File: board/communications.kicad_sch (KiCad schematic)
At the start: 8 parts, among them J1 RJ45_LED_Shielded, U3 ATA6561, U5 ATA6561

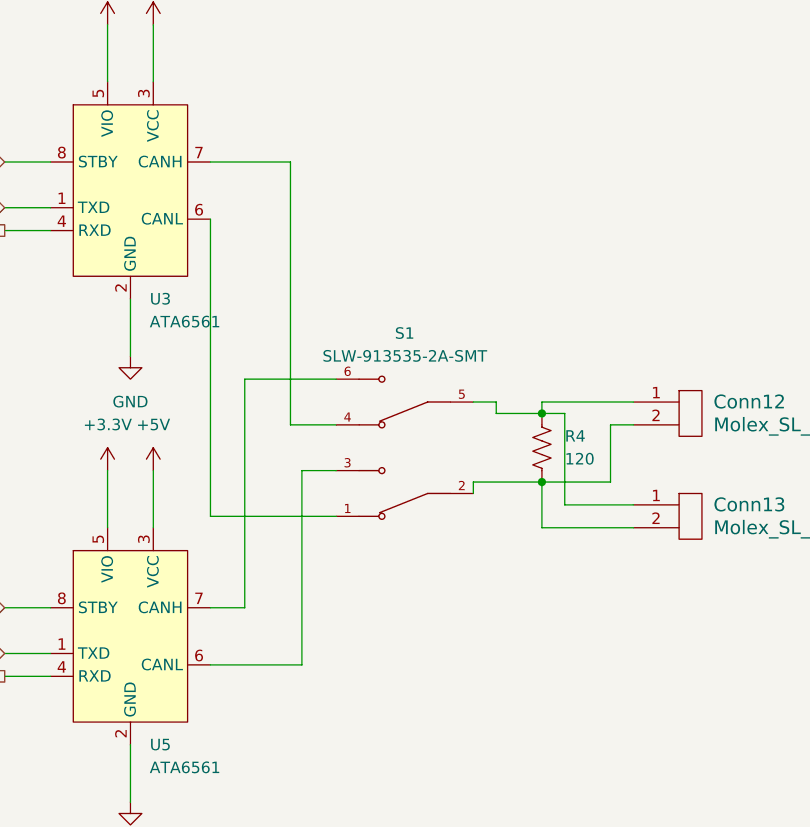
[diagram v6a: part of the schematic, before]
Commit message: Equalized traces, text resizing
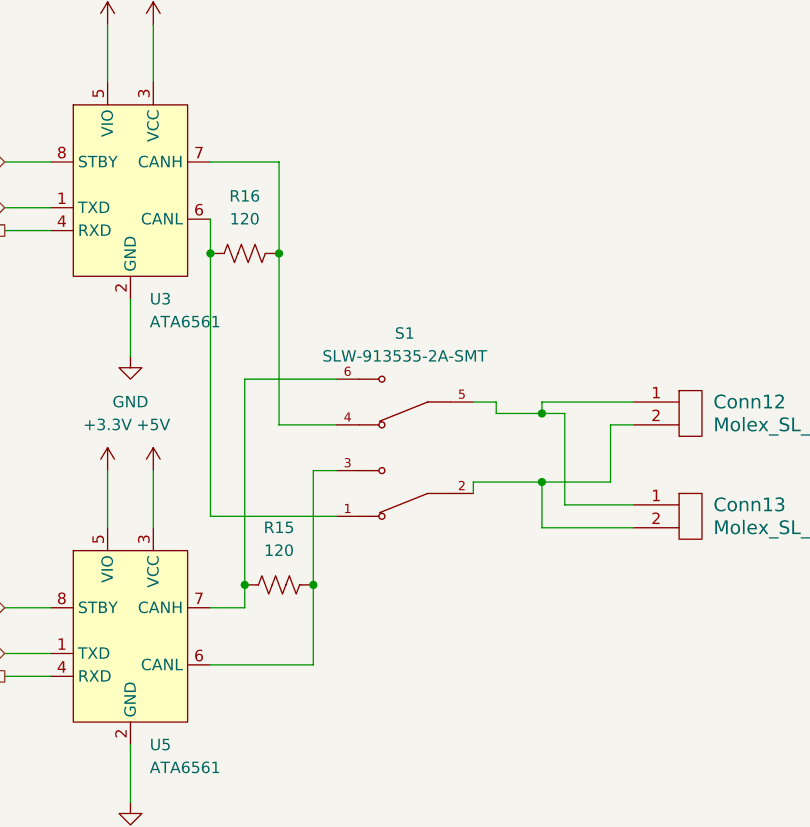
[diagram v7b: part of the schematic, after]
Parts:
- removed R4: 120, Resistor_SMD:R_0603_1608Metric_Pad0.98x0.95mm_HandSolder, symbol Device:R_US
- added R15, R16: 120, Resistor_SMD:R_0603_1608Metric_Pad0.98x0.95mm_HandSolder, symbol Device:R_US
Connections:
- net at S1.3, U5.6 (CANL): now also R15.1
- net at S1.6, U5.7 (CANH): now also R15.2
- net at S1.1, U3.6 (CANL): now also R16.2
- net at S1.4, U3.7 (CANH): now also R16.1
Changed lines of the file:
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@@
+	)
+	(junction
+		(at 123.19 58.42)
+		(diameter 0)
+		(color 0 0 0 0)
+	)
+	(junction
+		(at 130.81 58.42)
+		(diameter 0)
+		(color 0 0 0 0)
 	)
 	(junction
@@
 	)
 	(junction
+		(at 127 95.25)
+		(diameter 0)
+		(color 0 0 0 0)
+	)
+	(junction
 		(at 27.94 63.5)
+		(diameter 0)
+		(color 0 0 0 0)
+	)
+	(junction
+		(at 134.62 95.25)
 		(diameter 0)
 		(color 0 0 0 0)
@@
 	(wire
 		(pts
+			(xy 127 95.25) (xy 127 97.79)
+		)
+		(stroke
+			(width 0)
+			(type default)
+		)
+	)
+	(wire
+		(pts
 			(xy 160.02 88.9) (xy 170.18 88.9)
 		)
@@
 	(wire
 		(pts
-			(xy 127 72.39) (xy 127 97.79)
+			(xy 134.62 95.25) (xy 134.62 82.55)
+		)
+		(stroke
+			(width 0)
+			(type default)
+		)
+	)
+	(wire
+		(pts
+			(xy 127 72.39) (xy 127 95.25)
 		)
 		(stroke
@@
 	(wire
 		(pts
+			(xy 123.19 58.42) (xy 123.19 87.63)
+		)
+		(stroke
+			(width 0)
+			(type default)
+		)
+	)
+	(wire
+		(pts
 			(xy 160.02 76.2) (xy 162.56 76.2)
 		)
@@
 	(wire
 		(pts
-			(xy 123.19 54.61) (xy 123.19 87.63)
+			(xy 123.19 54.61) (xy 123.19 58.42)
 		)
 		(stroke
@@
 	(wire
 		(pts
-			(xy 133.35 82.55) (xy 137.16 82.55)
+			(xy 134.62 82.55) (xy 137.16 82.55)
 		)
 		(stroke
@@
 	(wire
 		(pts
-			(xy 132.08 77.47) (xy 137.16 77.47)
+			(xy 130.81 77.47) (xy 137.16 77.47)
 		)
 		(stroke
@@
 	(wire
 		(pts
-			(xy 123.19 48.26) (xy 132.08 48.26)
+			(xy 123.19 48.26) (xy 130.81 48.26)
 		)
 		(stroke
@@
 	(wire
 		(pts
-			(xy 133.35 104.14) (xy 133.35 82.55)
+			(xy 134.62 104.14) (xy 134.62 95.25)
 		)
 		(stroke
@@
 	(wire
 		(pts
+			(xy 130.81 58.42) (xy 130.81 77.47)
+		)
+		(stroke
+			(width 0)
+			(type default)
+		)
+	)
+	(wire
+		(pts
 			(xy 111.76 82.55) (xy 111.76 88.9)
 		)
@@
 	(wire
 		(pts
-			(xy 123.19 104.14) (xy 133.35 104.14)
+			(xy 123.19 104.14) (xy 134.62 104.14)
 		)
 		(stroke
@@
 	(wire
 		(pts
-			(xy 132.08 48.26) (xy 132.08 77.47)
+			(xy 130.81 48.26) (xy 130.81 58.42)
 		)
 		(stroke
@@
 	)
 	(symbol
+		(lib_id "Device:R_US")
+		(at 130.81 95.25 270)
+		(unit 1)
+		(exclude_from_sim no)
+		(in_bom yes)
+		(on_board yes)
+		(dnp no)
+		(fields_autoplaced yes)
+		(property "Reference" "R15"
+			(at 130.81 88.9 90)
+			(effects
+				(font
+					(size 1.27 1.27)
+				)
+			)
+		)
+		(property "Value" "120"
+			(at 130.81 91.44 90)
+			(effects
+				(font
+					(size 1.27 1.27)
+				)
+			)
+		)
+		(property "Footprint" "Resistor_SMD:R_0603_1608Metric_Pad0.98x0.95mm_HandSolder"
+			(at 130.556 96.266 90)
+			(effects
+				(font
+					(size 1.27 1.27)
+				)
+				(hide yes)
+			)
+		)
+		(property "Datasheet" "~"
+			(at 130.81 95.25 0)
+			(effects
+				(font
+					(size 1.27 1.27)
+				)
+				(hide yes)
+			)
+		)
+		(property "Description" "Resistor, US symbol"
+			(at 130.81 95.25 0)
+			(effects
+				(font
+					(size 1.27 1.27)
+				)
+				(hide yes)
+			)
+		)
+		(pin "1"
+		)
+		(pin "2"
+		)
+		(instances
+			(project "AugerBoard"
+				(path "/05fd3c2e-b986-4426-9c38-2a77d5c929de/2e8a1a4c-679b-4e28-aa1a-22908ea877e1"
+					(reference "R15")
+					(unit 1)
+				)
+			)
+		)
+	)
+	(symbol
 		(lib_id "MRDT_Switches:SLW-913535-2A-SMT")
 		(at 144.78 80.01 180)
@@
 	)
 	(symbol
-		(lib_id "Device:R_US")
-		(at 160.02 80.01 0)
-		(unit 1)
-		(exclude_from_sim no)
-		(in_bom yes)
-		(on_board yes)
-		(dnp no)
-		(fields_autoplaced yes)
-		(property "Reference" "R4"
-			(at 162.56 78.7399 0)
-			(effects
-				(font
-					(size 1.27 1.27)
-				)
-				(justify left)
-			)
-		)
-		(property "Value" "120"
-			(at 162.56 81.2799 0)
-			(effects
-				(font
-					(size 1.27 1.27)
-				)
-				(justify left)
-			)
-		)
-		(property "Footprint" "Resistor_SMD:R_0603_1608Metric_Pad0.98x0.95mm_HandSolder"
-			(at 161.036 80.264 90)
-			(effects
-				(font
-					(size 1.27 1.27)
-				)
-				(hide yes)
-			)
-		)
-		(property "Datasheet" "~"
-			(at 160.02 80.01 0)
-			(effects
-				(font
-					(size 1.27 1.27)
-				)
-				(hide yes)
-			)
-		)
-		(property "Description" "Resistor, US symbol"
-			(at 160.02 80.01 0)
-			(effects
-				(font
-					(size 1.27 1.27)
-				)
-				(hide yes)
-			)
-		)
-		(pin "1"
-		)
-		(pin "2"
-		)
-		(instances
-			(project ""
-				(path "/05fd3c2e-b986-4426-9c38-2a77d5c929de/2e8a1a4c-679b-4e28-aa1a-22908ea877e1"
-					(reference "R4")
-					(unit 1)
-				)
-			)
-		)
-	)
-	(symbol
 		(lib_id "Connector:RJ45_LED_Shielded")
 		(at 46.99 40.64 270)
@@
 					(unit 1)
 				)
+			)
+		)
+	)
+	(symbol
+		(lib_id "Device:R_US")
+		(at 127 58.42 270)
+		(unit 1)
+		(exclude_from_sim no)
+		(in_bom yes)
+		(on_board yes)
+		(dnp no)
+		(fields_autoplaced yes)
+		(property "Reference" "R16"
+			(at 127 52.07 90)
+			(effects
+				(font
+					(size 1.27 1.27)
+				)
+			)
+		)
+		(property "Value" "120"
+			(at 127 54.61 90)
+			(effects
+				(font
+					(size 1.27 1.27)
+				)
+			)
+		)
+		(property "Footprint" "Resistor_SMD:R_0603_1608Metric_Pad0.98x0.95mm_HandSolder"
+			(at 126.746 59.436 90)
+			(effects
+				(font
+					(size 1.27 1.27)
+				)
+				(hide yes)
+			)
+		)
+		(property "Datasheet" "~"
+			(at 127 58.42 0)
+			(effects
+				(font
+					(size 1.27 1.27)
+				)
+				(hide yes)
+			)
+		)
+		(property "Description" "Resistor, US symbol"
+			(at 127 58.42 0)
+			(effects
+				(font
+					(size 1.27 1.27)
+				)
+				(hide yes)
+			)
+		)
+		(pin "1"
+		)
+		(pin "2"
+		)
+		(instances
+			(project "AugerBoard"
+				(path "/05fd3c2e-b986-4426-9c38-2a77d5c929de/2e8a1a4c-679b-4e28-aa1a-22908ea877e1"
+					(reference "R16")
+					(unit 1)
+				)
